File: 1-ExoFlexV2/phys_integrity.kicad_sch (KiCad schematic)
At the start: 30 parts, among them J76 100k, J77 100k, J78 100k, J79 100k, J80 100k, J81 100k, U69 SN74LVC1G32DBVR, U70 SN74LVC1G32DBVR, U71 SN74LVC1G32DBVR, U72 SN74LVC1G32DBVR, U73 SN74LVC1G32DBVR

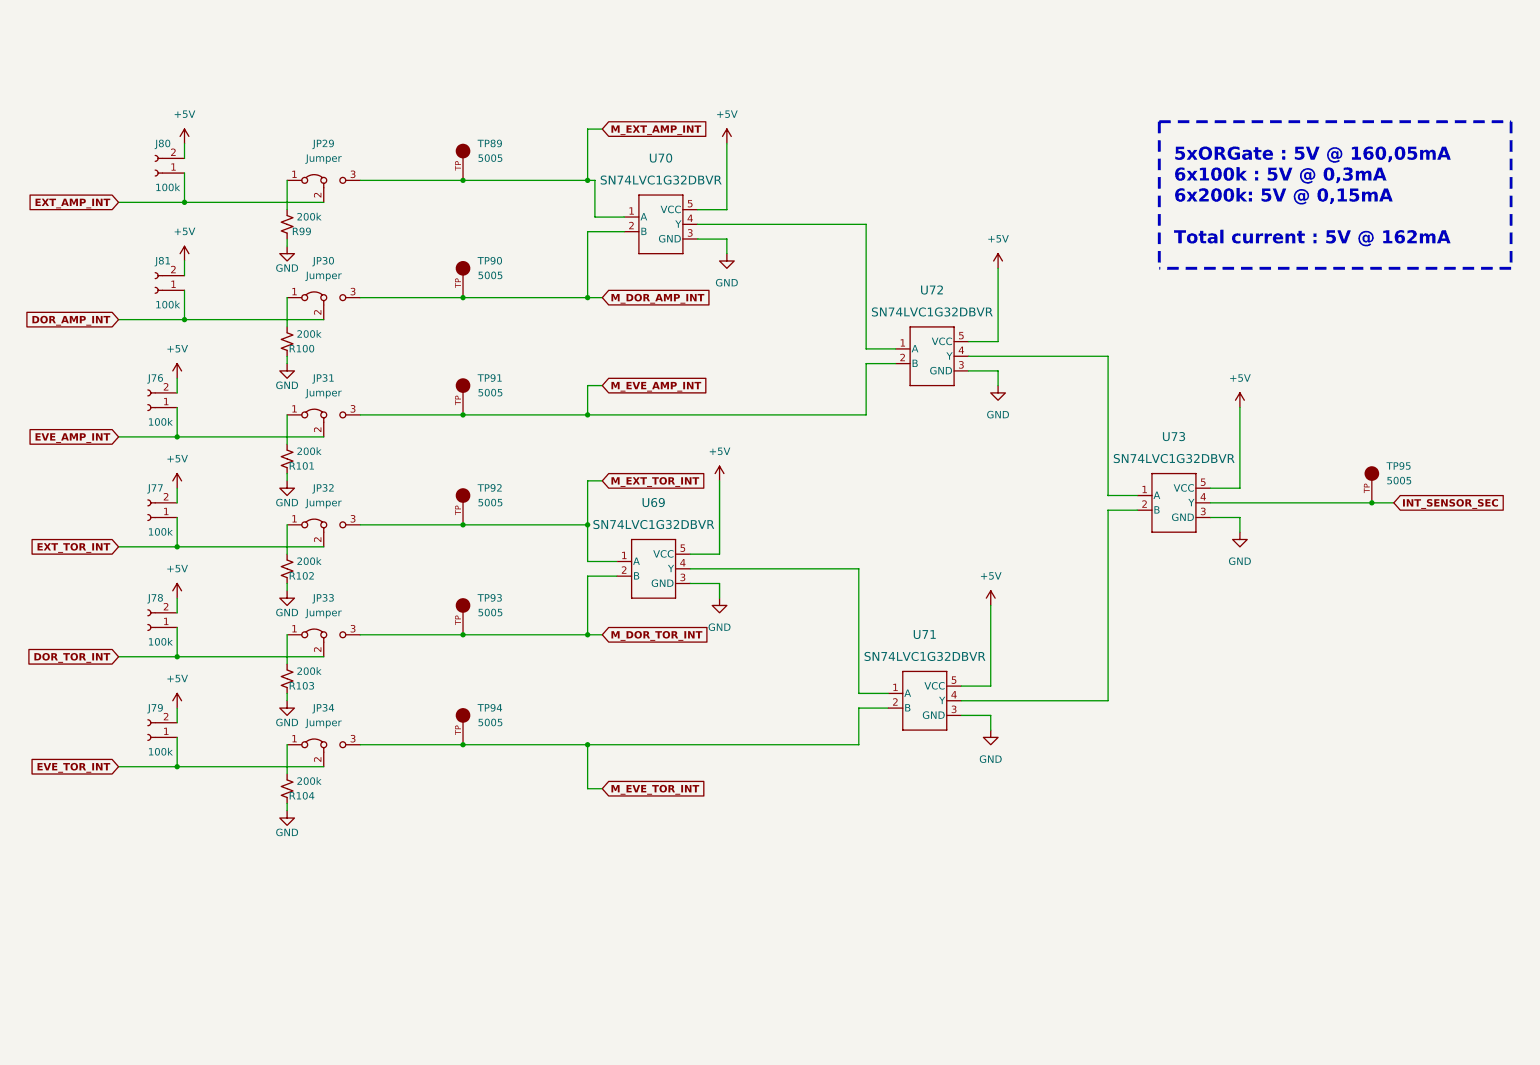
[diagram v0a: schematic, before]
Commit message: Chokes et RC
- Ajout des RF chokes
- Changement des résistance pour 0805
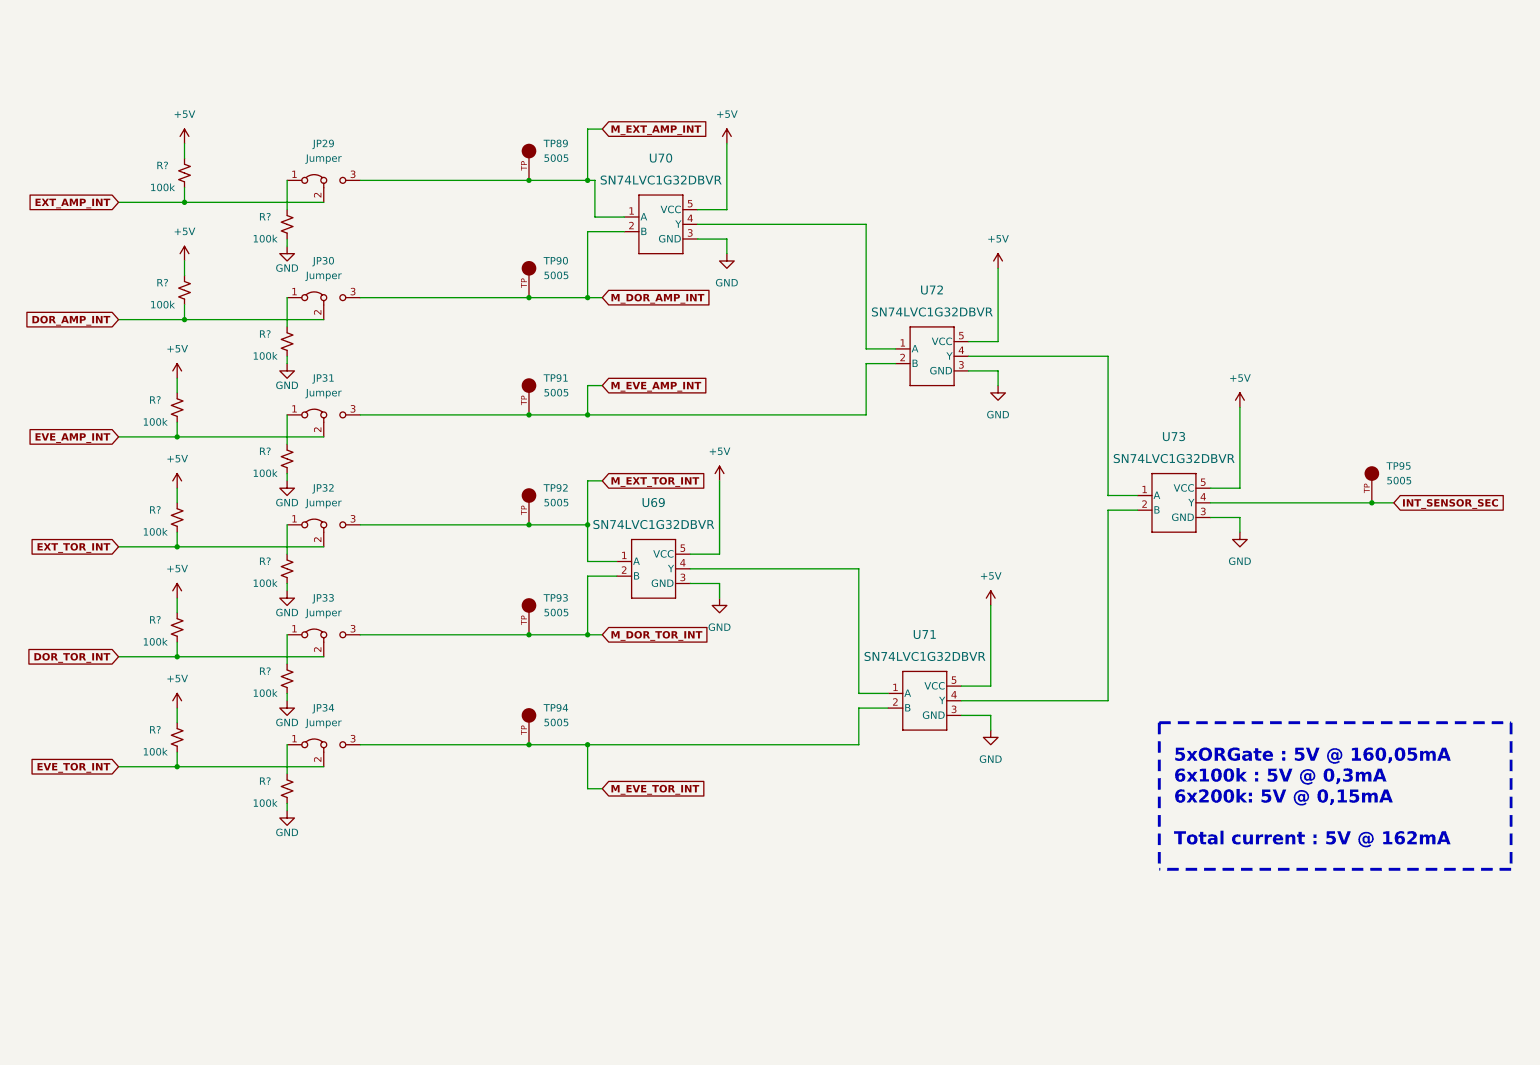
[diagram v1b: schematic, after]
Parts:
- removed J76, J77, J78, J79, J80, J81: 100k, Connector_PinHeader_2.54mm:PinHeader_1x02_P2.54mm_Vertical, symbol Connector:Conn_01x02_Female
- removed R100, R101, R102, R103, R104, R99: 200k, Resistor_SMD:R_0603_1608Metric, symbol Device:R_Small_US
- added R? (x12): 100k, Resistor_SMD:R_0805_2012Metric, symbol Device:R_Small_US
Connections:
- net +5V: now also R?.1, R?.1, R?.1, R?.1, R?.1, R?.1
- net DOR_AMP_INT: now also R?.2
- net DOR_TOR_INT: now also R?.2
- net EVE_AMP_INT: now also R?.2
- net EVE_TOR_INT: now also R?.2
- net EXT_AMP_INT: now also R?.2
- net EXT_TOR_INT: now also R?.2
- net GND: now also R?.2, R?.2, R?.2, R?.2, R?.2, R?.2
- net at JP29.1 (A): now also R?.1
- net at JP34.1 (A): now also R?.1
- net at JP33.1 (A): now also R?.1
- net at JP32.1 (A): now also R?.1
- net at JP30.1 (A): now also R?.1
- net at JP31.1 (A): now also R?.1
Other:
- moved on the sheet: TP89, TP90, TP91, TP92, TP93, TP94

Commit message: Trimmer et jumper
-Changement de symbole de jumper
-Ajout des des trimmer aux endroits nécessaires
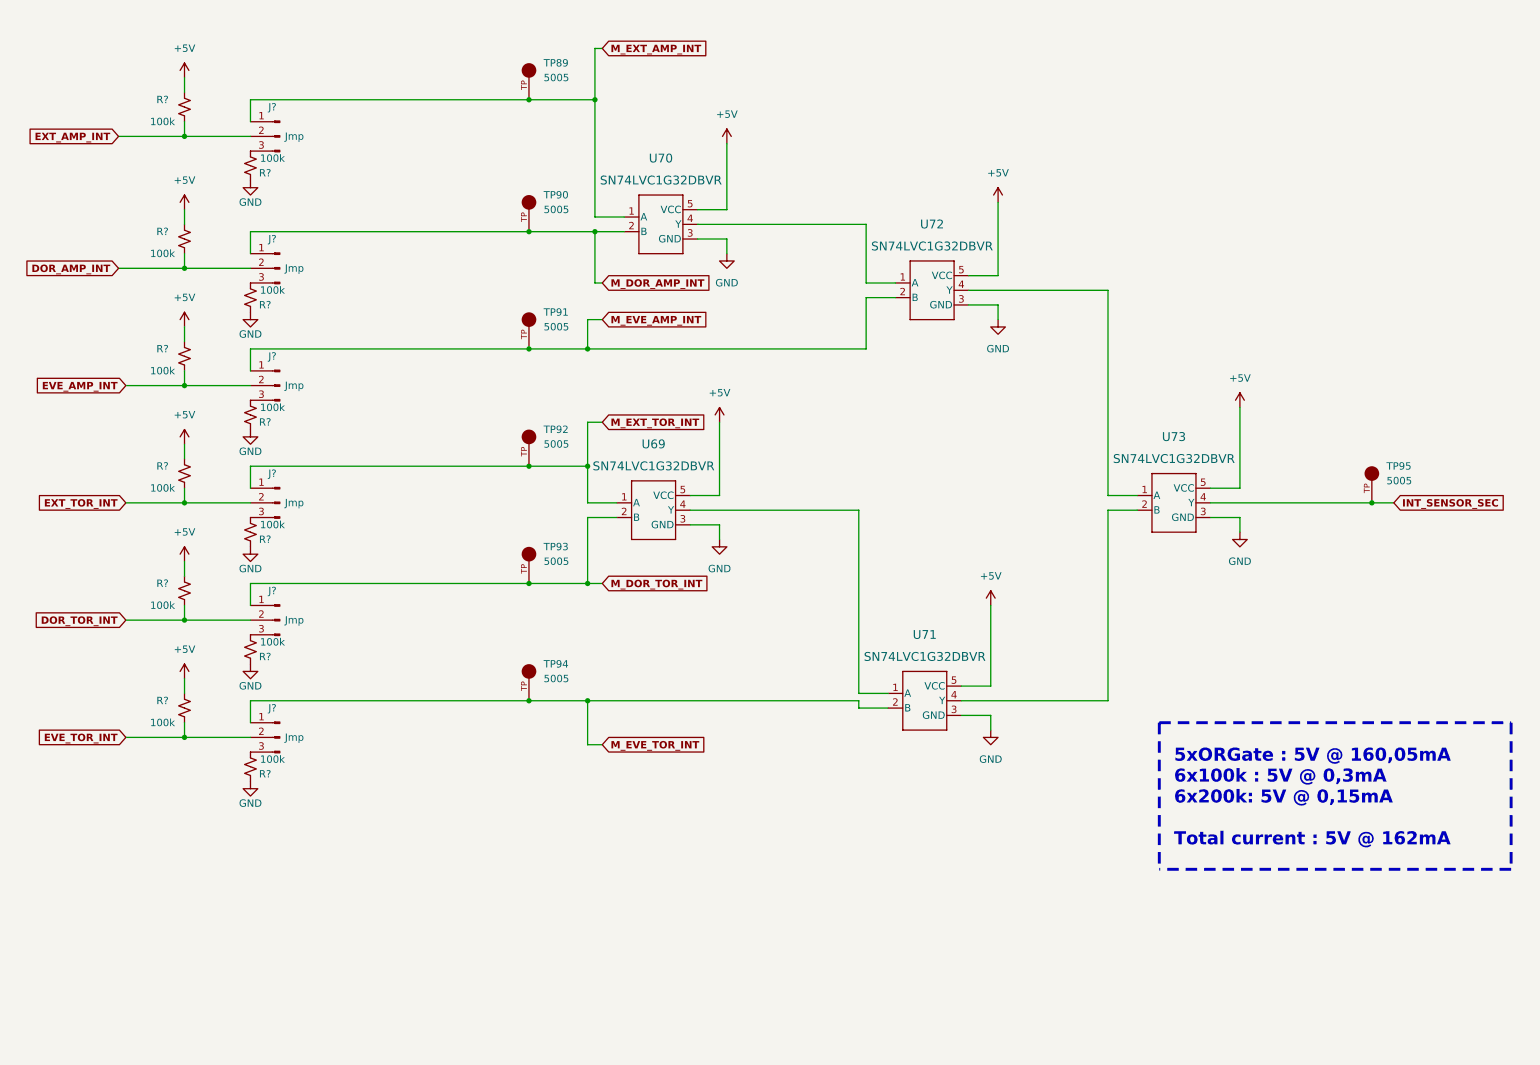
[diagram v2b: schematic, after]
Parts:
- removed JP29, JP30, JP31, JP32, JP33, JP34: Jumper, Connector_PinHeader_2.54mm:PinHeader_1x03_P2.54mm_Vertical, symbol Jumper:Jumper_3_Bridged12
- removed R? (x6): 100k, Resistor_SMD:R_0805_2012Metric, symbol Device:R_Small_US
- added J? (x6): Jmp, symbol Connector:Conn_01x03_Male
- added R? (x6): 100k, Resistor_SMD:R_0805_2012Metric, symbol Device:R_Small_US
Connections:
- net DOR_AMP_INT: now also J?.2 (Pin_2)
- net DOR_TOR_INT: now also J?.2 (Pin_2)
- net EVE_AMP_INT: now also J?.2 (Pin_2)
- net EVE_TOR_INT: now also J?.2 (Pin_2)
- net EXT_AMP_INT: now also J?.2 (Pin_2)
- net EXT_TOR_INT: now also J?.2 (Pin_2)
- net GND: now also R?.2, R?.2, R?.2, R?.2, R?.2, R?.2
- net M_DOR_AMP_INT: now also J?.1 (Pin_1)
- net M_DOR_TOR_INT: now also J?.1 (Pin_1)
- net M_EVE_AMP_INT: now also J?.1 (Pin_1)
- net M_EVE_TOR_INT: now also J?.1 (Pin_1)
- net M_EXT_AMP_INT: now also J?.1 (Pin_1)
- net M_EXT_TOR_INT: now also J?.1 (Pin_1)
- new net: J?.3 (Pin_3), R?.1 (x6)
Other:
- moved on the sheet: R?, TP89, TP90, TP91, TP92, TP93, TP94, U69, U72

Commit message: Test points et notes
- Ajout de tous les tests point nécessaires
-  Ajoute des sections de notes dans chaque page
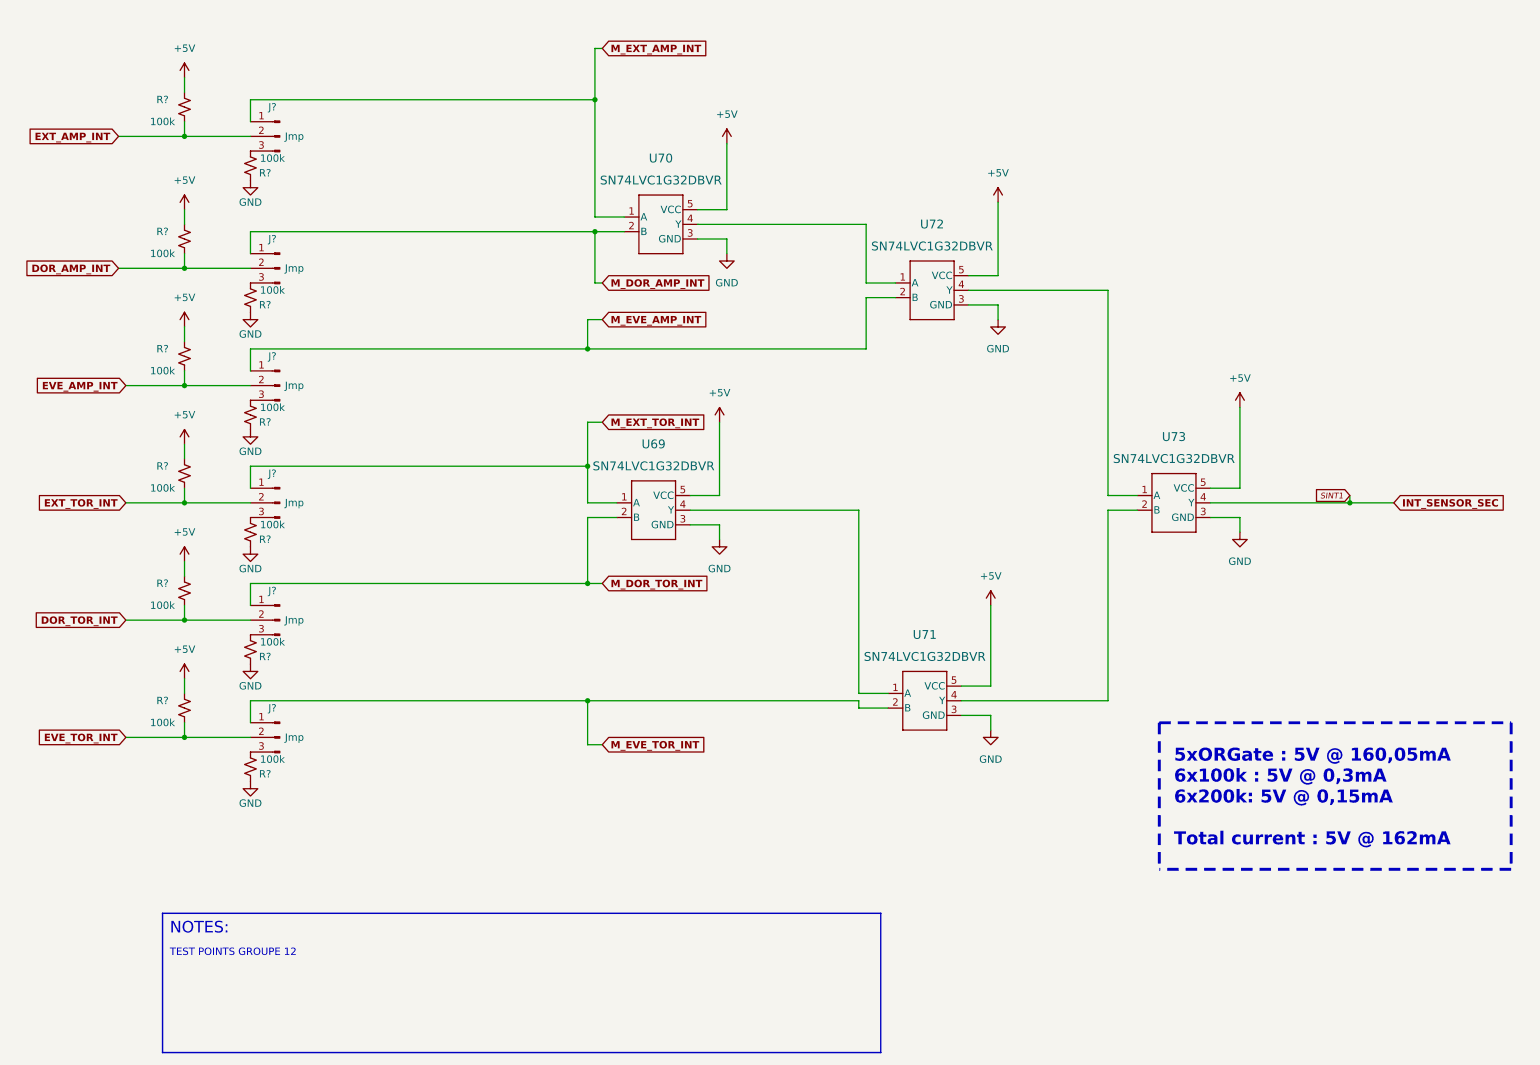
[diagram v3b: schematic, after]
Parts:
- removed TP89, TP90, TP91, TP92, TP93, TP94, TP95: 5005, FootPrint:KEYSTONE_5005, symbol SymLib:5005
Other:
- note added: "NOTES:"
- note added: "TEST POINTS GROUPE 12"

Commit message: Schématisation terminée
- Schéma terminé
- Passage vers le PCB
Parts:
- J111, J112, J113, J114, J115, J116: renamed from J?; value Jmp -> Jumper; footprint (none) -> Connector_PinSocket_2.54mm:PinSocket_1x03_P2.54mm_Vertical; DESCRIPTION (none) -> CONN HEADER VERT 3POS 2.54MM; MANUFACTURER (none) -> Würth Elektronik; PACKAGE (none) -> Square 0.100" (2.54mm); PART NUMBER (none) -> 61300311121; TYPE (none) -> Through Hole
- R170, R171, R172, R173, R174, R175, R176, R177, R178, R179, R180, R181: renamed from R?; value 100k -> 100k 5% 1/8W; DESCRIPTION (none) -> 100 kOhms ±5% 0.125W, 1/8W Chip Resistor 0805 (2012 Metric)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; MANUFACTURER (none) -> Panasonic Electronic Components; PACKAGE (none) -> 0805 (2012 Metric); PART NUMBER (none) -> ERJ-6GEYJ104V; TYPE (none) -> SMD
- U88: renamed from U69; value SN74LVC1G32DBVR -> OR Gate; DESCRIPTION (none) -> OR Gate IC 1 Channel SOT-23-5; MANUFACTURER (none) -> Texas Instruments; PACKAGE (none) -> SC-74A, SOT-753; PART NUMBER (none) -> SN74LVC1G32DBVR; TYPE (none) -> SMD
- U89: renamed from U70; value SN74LVC1G32DBVR -> OR Gate; DESCRIPTION (none) -> OR Gate IC 1 Channel SOT-23-5; MANUFACTURER (none) -> Texas Instruments; PACKAGE (none) -> SC-74A, SOT-753; PART NUMBER (none) -> SN74LVC1G32DBVR; TYPE (none) -> SMD
- U90: renamed from U71; value SN74LVC1G32DBVR -> OR Gate; DESCRIPTION (none) -> OR Gate IC 1 Channel SOT-23-5; MANUFACTURER (none) -> Texas Instruments; PACKAGE (none) -> SC-74A, SOT-753; PART NUMBER (none) -> SN74LVC1G32DBVR; TYPE (none) -> SMD
- U91: renamed from U72; value SN74LVC1G32DBVR -> OR Gate; DESCRIPTION (none) -> OR Gate IC 1 Channel SOT-23-5; MANUFACTURER (none) -> Texas Instruments; PACKAGE (none) -> SC-74A, SOT-753; PART NUMBER (none) -> SN74LVC1G32DBVR; TYPE (none) -> SMD
- U92: renamed from U73; value SN74LVC1G32DBVR -> OR Gate; DESCRIPTION (none) -> OR Gate IC 1 Channel SOT-23-5; MANUFACTURER (none) -> Texas Instruments; PACKAGE (none) -> SC-74A, SOT-753; PART NUMBER (none) -> SN74LVC1G32DBVR; TYPE (none) -> SMD
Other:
- note added: "5xORGate : 5V @ 160,05mA 12x100k : 5V @ 0,6mA Total current : 5V @ 165mA"
- note removed: "5xORGate : 5V @ 160,05mA 6x100k : 5V @ 0,3mA 6x200k: 5V @ 0,15mA Total current : 5V @ 162mA"
- moved on the sheet: R170, R171, R172, R173, R174, R175
